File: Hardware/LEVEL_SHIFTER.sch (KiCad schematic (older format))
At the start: 61 parts, among them U11 GTL2010, U12 GTL2010, U13 GTL2010

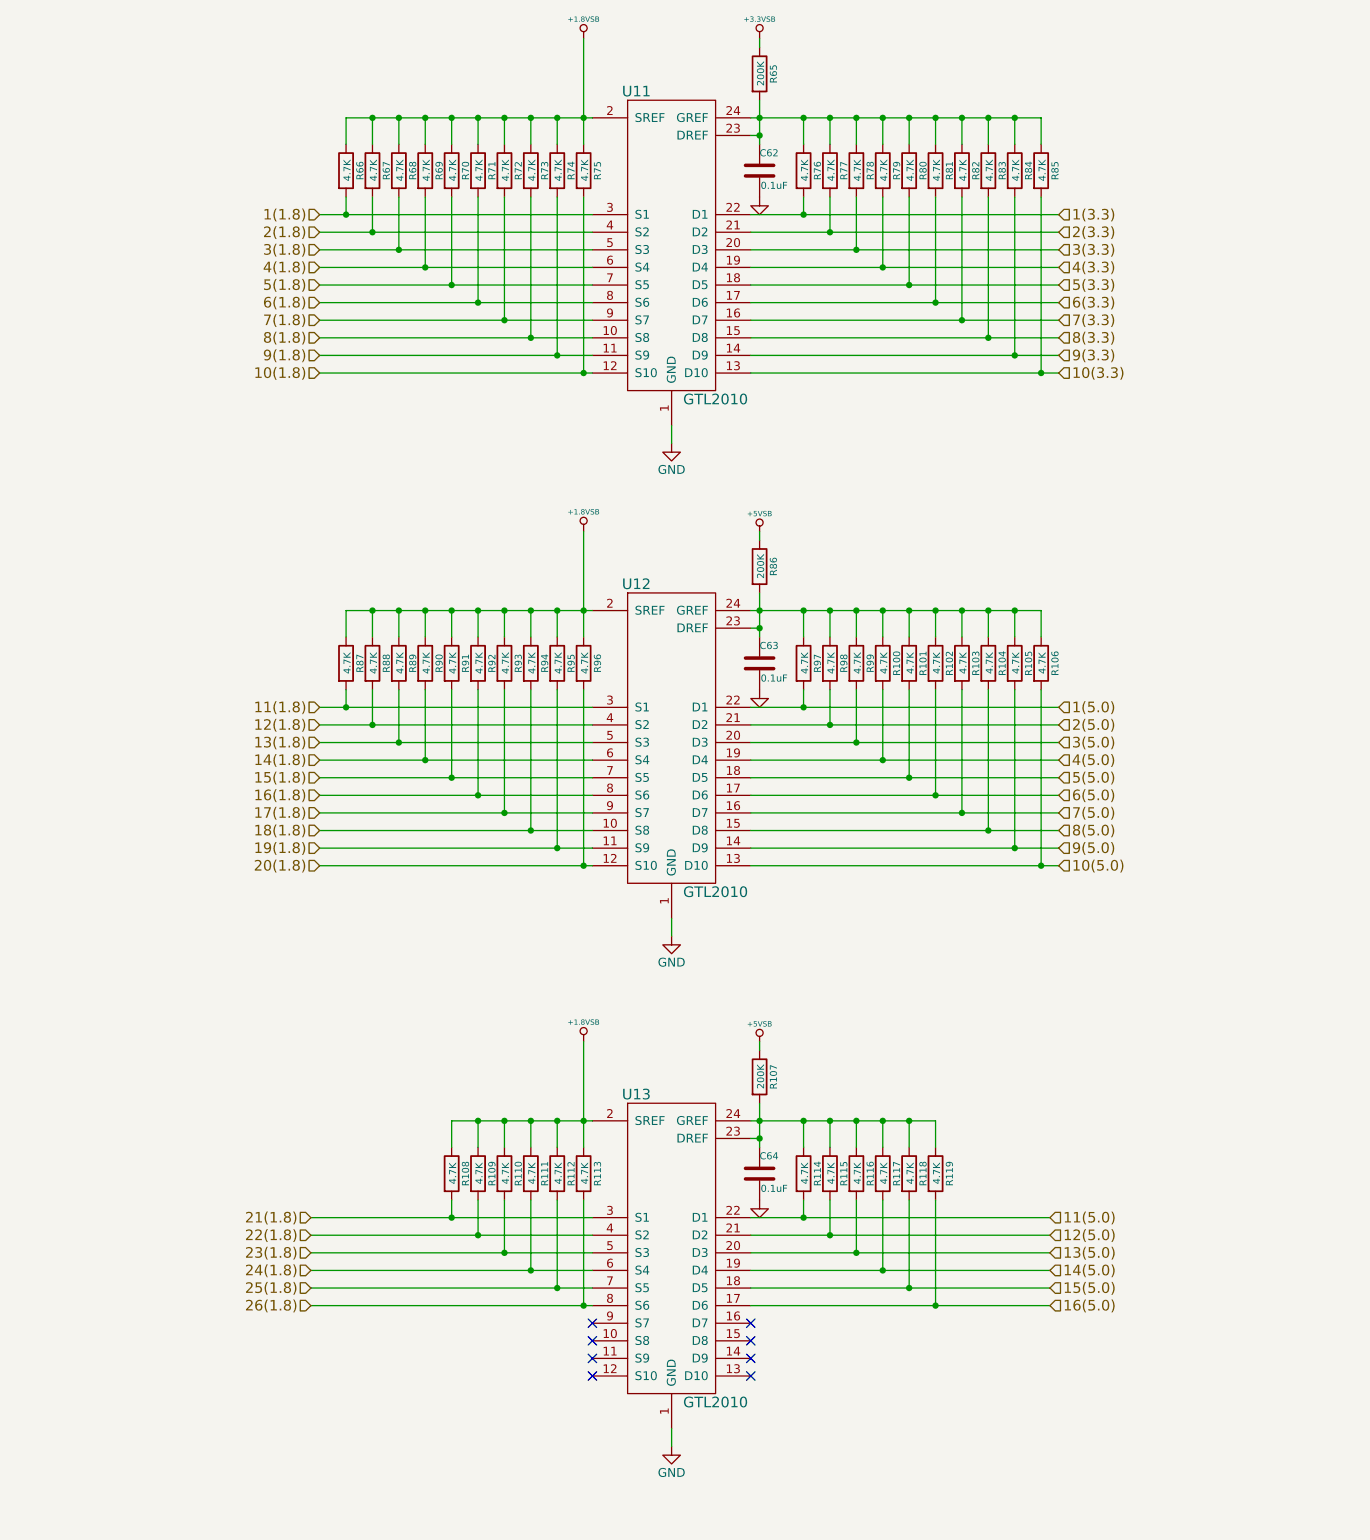
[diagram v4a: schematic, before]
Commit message: Finished converting to global labels
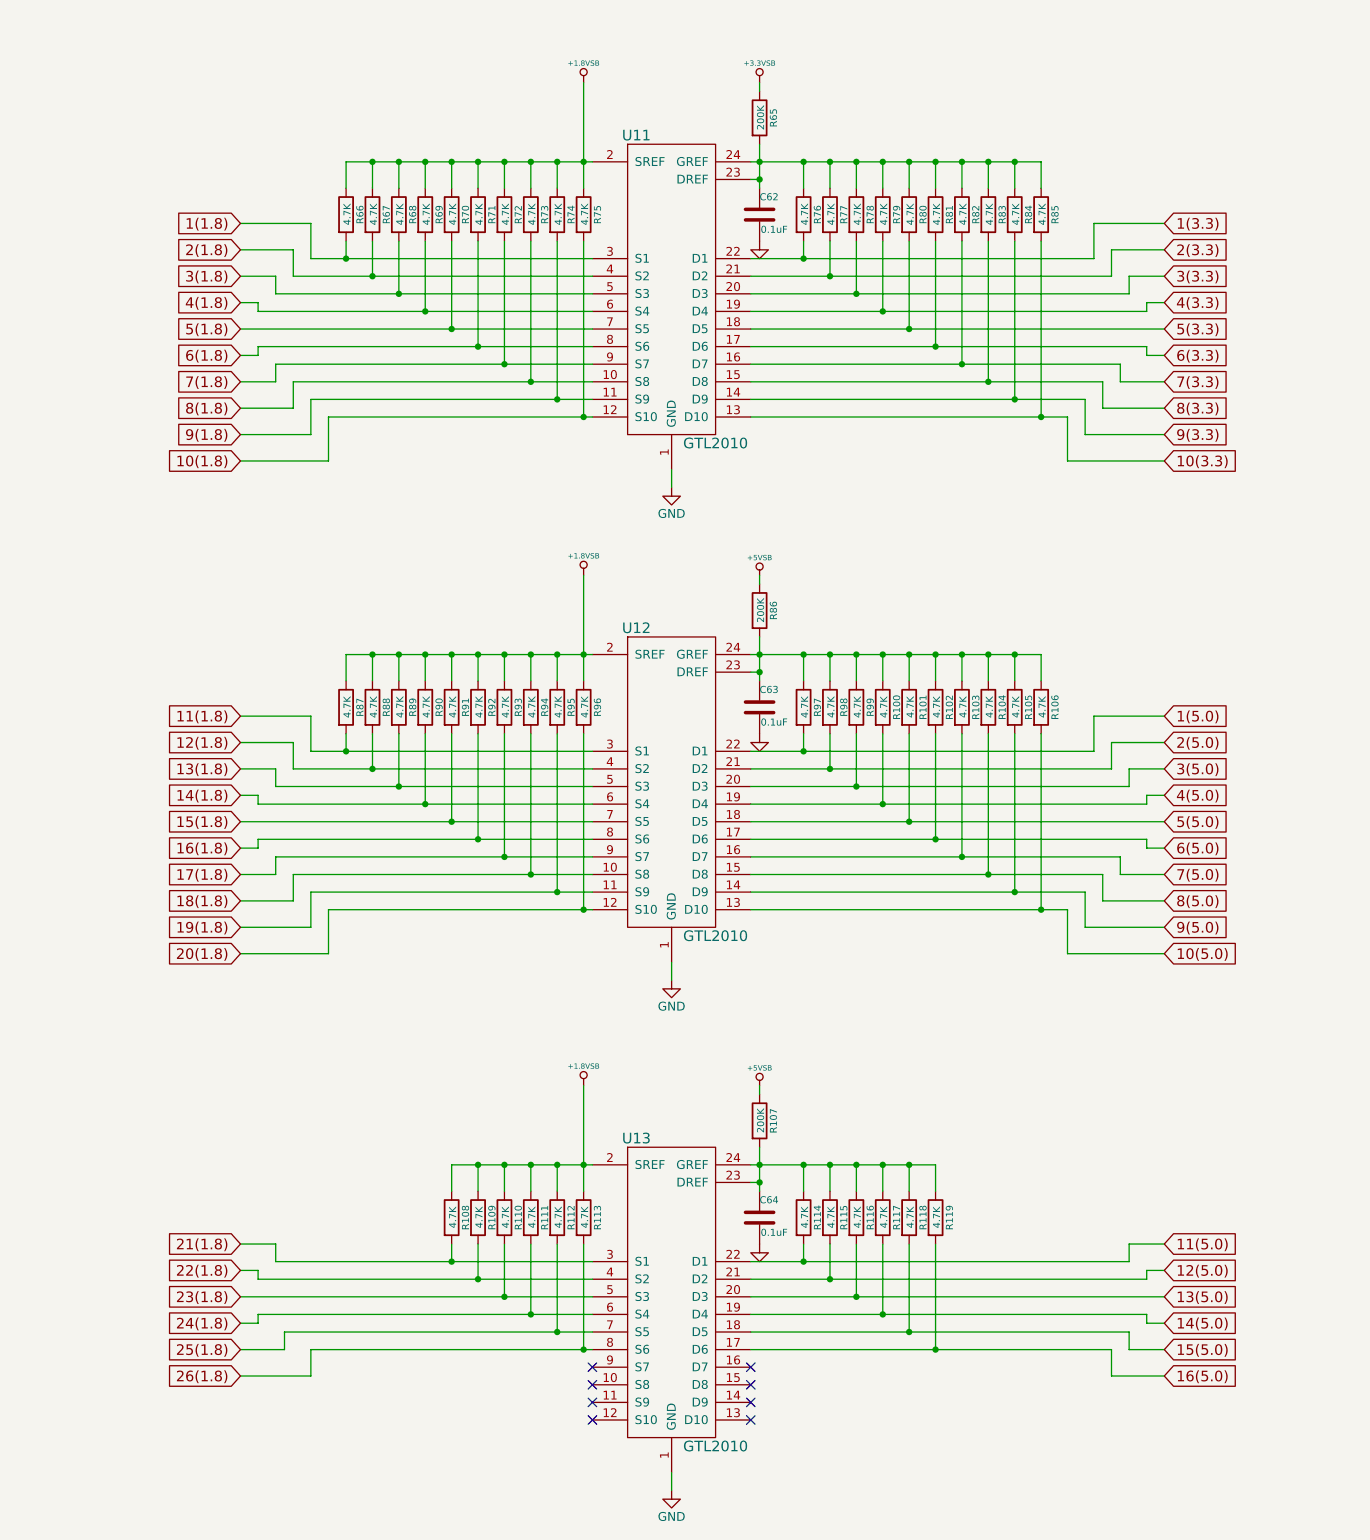
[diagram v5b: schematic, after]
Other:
- moved on the sheet: C62, C63, C64, R100, R101, R102, R103, R104, R105, R106, R107, R108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

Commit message: Updated I2C pullup resistors and labels
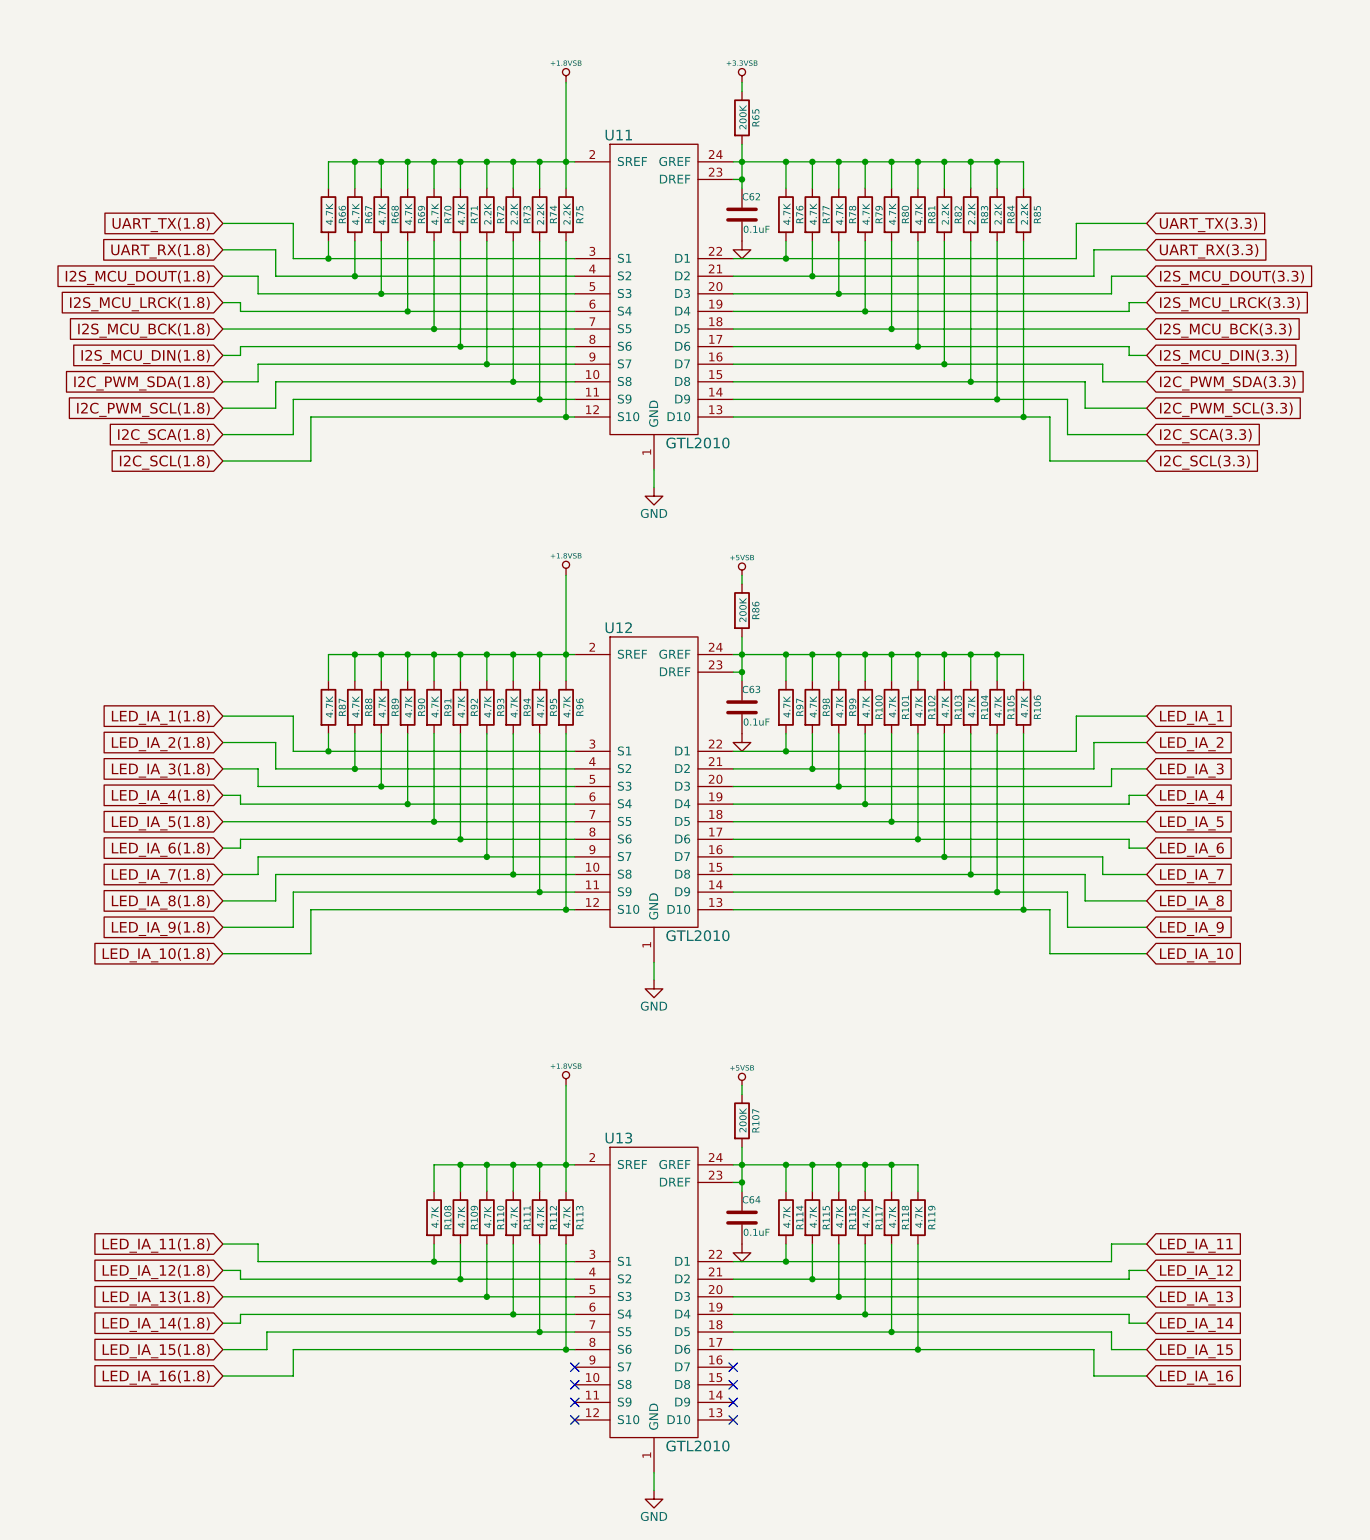
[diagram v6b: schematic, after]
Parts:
- R72, R73, R74, R75, R82, R83, R84, R85: value 4.7K -> 2.2K
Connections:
- net 1(1.8) renamed UART_TX(1.8)
- net 1(3.3) renamed UART_TX(3.3)
- net 1(5.0) renamed LED_IA_1
- net 10(1.8) renamed I2C_SCL(1.8)
- net 10(3.3) renamed I2C_SCL(3.3)
- net 10(5.0) renamed LED_IA_10
- net 11(1.8) renamed LED_IA_1(1.8)
- net 11(5.0) renamed LED_IA_11
- net 12(1.8) renamed LED_IA_2(1.8)
- net 12(5.0) renamed LED_IA_12
- net 13(1.8) renamed LED_IA_3(1.8)
- net 13(5.0) renamed LED_IA_13
- net 14(1.8) renamed LED_IA_4(1.8)
- net 14(5.0) renamed LED_IA_14
- net 15(1.8) renamed LED_IA_5(1.8)
- net 15(5.0) renamed LED_IA_15
- net 16(1.8) renamed LED_IA_6(1.8)
- net 16(5.0) renamed LED_IA_16
- net 17(1.8) renamed LED_IA_7(1.8)
- net 18(1.8) renamed LED_IA_8(1.8)
- net 19(1.8) renamed LED_IA_9(1.8)
- net 2(1.8) renamed UART_RX(1.8)
- net 2(3.3) renamed UART_RX(3.3)
- net 2(5.0) renamed LED_IA_2
- net 20(1.8) renamed LED_IA_10(1.8)
- net 21(1.8) renamed LED_IA_11(1.8)
- net 22(1.8) renamed LED_IA_12(1.8)
- net 23(1.8) renamed LED_IA_13(1.8)
- net 24(1.8) renamed LED_IA_14(1.8)
- net 25(1.8) renamed LED_IA_15(1.8)
- net 26(1.8) renamed LED_IA_16(1.8)
- net 3(1.8) renamed I2S_MCU_DOUT(1.8)
- net 3(3.3) renamed I2S_MCU_DOUT(3.3)
- net 3(5.0) renamed LED_IA_3
- net 4(1.8) renamed I2S_MCU_LRCK(1.8)
- net 4(3.3) renamed I2S_MCU_LRCK(3.3)
- net 4(5.0) renamed LED_IA_4
- net 5(1.8) renamed I2S_MCU_BCK(1.8)
- net 5(3.3) renamed I2S_MCU_BCK(3.3)
- net 5(5.0) renamed LED_IA_5
- net 6(1.8) renamed I2S_MCU_DIN(1.8)
- net 6(3.3) renamed I2S_MCU_DIN(3.3)
- net 6(5.0) renamed LED_IA_6
- net 7(1.8) renamed I2C_PWM_SDA(1.8)
- net 7(3.3) renamed I2C_PWM_SDA(3.3)
- net 7(5.0) renamed LED_IA_7
- net 8(1.8) renamed I2C_PWM_SCL(1.8)
- net 8(3.3) renamed I2C_PWM_SCL(3.3)
- net 8(5.0) renamed LED_IA_8
- net 9(1.8) renamed I2C_SCA(1.8)
- net 9(3.3) renamed I2C_SCA(3.3)
- net 9(5.0) renamed LED_IA_9
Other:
- moved on the sheet: C62, C63, C64, R100, R101, R102, R103, R104, R105, R106, R107, R108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

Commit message: Made design review fixes, added breakouts
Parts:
- removed C64: 0.1uF, symbol C-RESCUE-museV2
- removed R107: 200K, symbol R-RESCUE-museV2
- removed R108, R109, R110, R111, R112, R113, R114, R115, R116, R117, R118, R119: 4.7K, symbol R-RESCUE-museV2
- added C?: 0.1uF, symbol C-RESCUE-museV2
- added R?: 200K, symbol R-RESCUE-museV2
- added R? (x16): 4.7K, symbol R-RESCUE-museV2
- added R? (x8): 0, symbol R-RESCUE-museV2
- renumbered C62 to C80, C63 to C81, R66 to R44, R87 to R45, R67 to R46, R88 to R47, R68 to R48, R89 to R49, R69 to R50, R90 to R51, R70 to R52, R91 to R53, R71 to R55, R92 to R56, R72 to R58, R93 to R59, R73 to R61, R94 to R62, R74 to R64, R95 to R65, R75 to R67, R96 to R68, R65 to R70, R86 to R71, R76 to R73, R97 to R74, R77 to R76, R98 to R77, R78 to R79, R99 to R80, R79 to R82, R100 to R83, R80 to R85, R101 to R86, R81 to R88, R102 to R89, R82 to R91, R103 to R92, R83 to R93, R104 to R94, R84 to R95, R105 to R96, R85 to R97, R106 to R98, U11 to U19, U12 to U20, U13 to U21
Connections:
- net +1.8VSB: now also R?.1, R?.1, R?.1, R?.1, R?.1, R?.1, R?.1, R?.1, R?.1, R?.1
- net +3.3VSB: now also R?.1, R?.1, R?.1, R?.1
- net +5VSB: now also R?.1, R?.1, R?.1, R?.1, R?.1
- net GND: now also C?.2
- net LED_IA_11: now also R?.2
- net LED_IA_11(1.8): now also R?.2
- net LED_IA_12: now also R?.2
- net LED_IA_12(1.8): now also R?.2
- net LED_IA_13: now also R?.2
- net LED_IA_13(1.8): now also R?.2
- net LED_IA_14: now also R?.2
- net LED_IA_14(1.8): now also R?.2
- net LED_IA_15: now also R?.2
- net LED_IA_15(1.8): now also R?.2
- net LED_IA_16: now also R?.2
- net LED_IA_16(1.8): now also R?.2
- net at U21.23 (DREF), U21.24 (GREF): now also C?.1, R?.1, R?.1, R?.1, R?.1, R?.1, R?.1, R?.2
- net LVL_SHIFT_2(1.8): now reaches U21.10 (S8)
- net LVL_SHIFT_2(1.8): now also R?.2
- net LVL_SHIFT_3(1.8): now reaches U21.11 (S9)
- net LVL_SHIFT_3(1.8): now also R?.2
- net LVL_SHIFT_4(1.8): now reaches U21.12 (S10)
- net LVL_SHIFT_4(1.8): now also R?.2
- net LVL_SHIFT_4: now reaches U21.13 (D10)
- net LVL_SHIFT_4: now also R?.2, R?.2
- net LVL_SHIFT_3: now reaches U21.14 (D9)
- net LVL_SHIFT_3: now also R?.2, R?.2
- net LVL_SHIFT_2: now reaches U21.15 (D8)
- net LVL_SHIFT_2: now also R?.2, R?.2
- net LVL_SHIFT_1: now reaches U21.16 (D7)
- net LVL_SHIFT_1: now also R?.2, R?.2
- net LVL_SHIFT_1(1.8): now reaches U21.9 (S7)
- net LVL_SHIFT_1(1.8): now also R?.2
- no-connect marks 8 -> 0
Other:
- note added: "Selectable pullup voltage"

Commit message: Annotated schematic
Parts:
- gave numbers to parts that had none: 26
- renumbered C80 to C78, C81 to C79, R70 to R44, R44 to R45, R48 to R47, R50 to R48, R52 to R49, R55 to R50, R58 to R51, R61 to R52, R64 to R53, R67 to R54, R73 to R55, R76 to R56, R79 to R57, R82 to R58, R85 to R59, R88 to R60, R91 to R61, R93 to R62, R95 to R63, R97 to R64, R71 to R65, R45 to R66, R47 to R67, R49 to R68, R51 to R69, R53 to R70, R56 to R71, R59 to R72, R62 to R73, R65 to R74, R68 to R75, R74 to R76, R80 to R78, R83 to R79, R86 to R80, R89 to R81, R92 to R82, R94 to R83, R96 to R84, R98 to R85
